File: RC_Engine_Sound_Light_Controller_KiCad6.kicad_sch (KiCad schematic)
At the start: 35 parts, among them J1 RX, J10 RGB, J11 32, J12 CH1, J13 CH2, J14 CH3, J15 ESC, J16 CH4, J2 HeadL, J3 TailL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

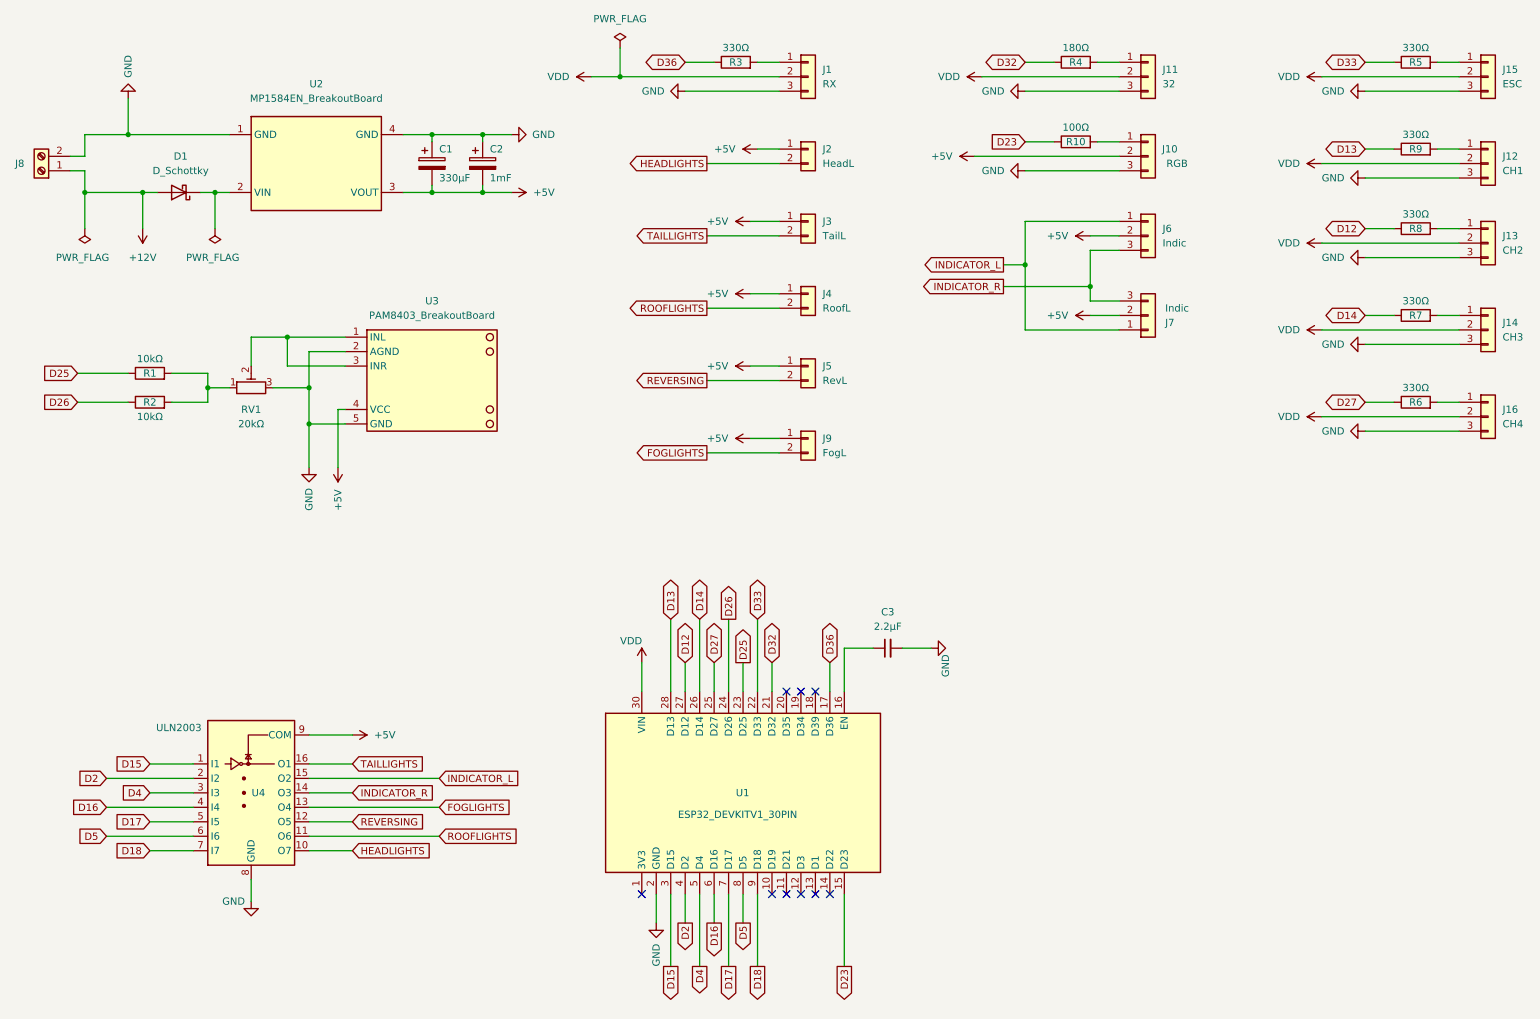
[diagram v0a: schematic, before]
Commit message: Added VDD diode.
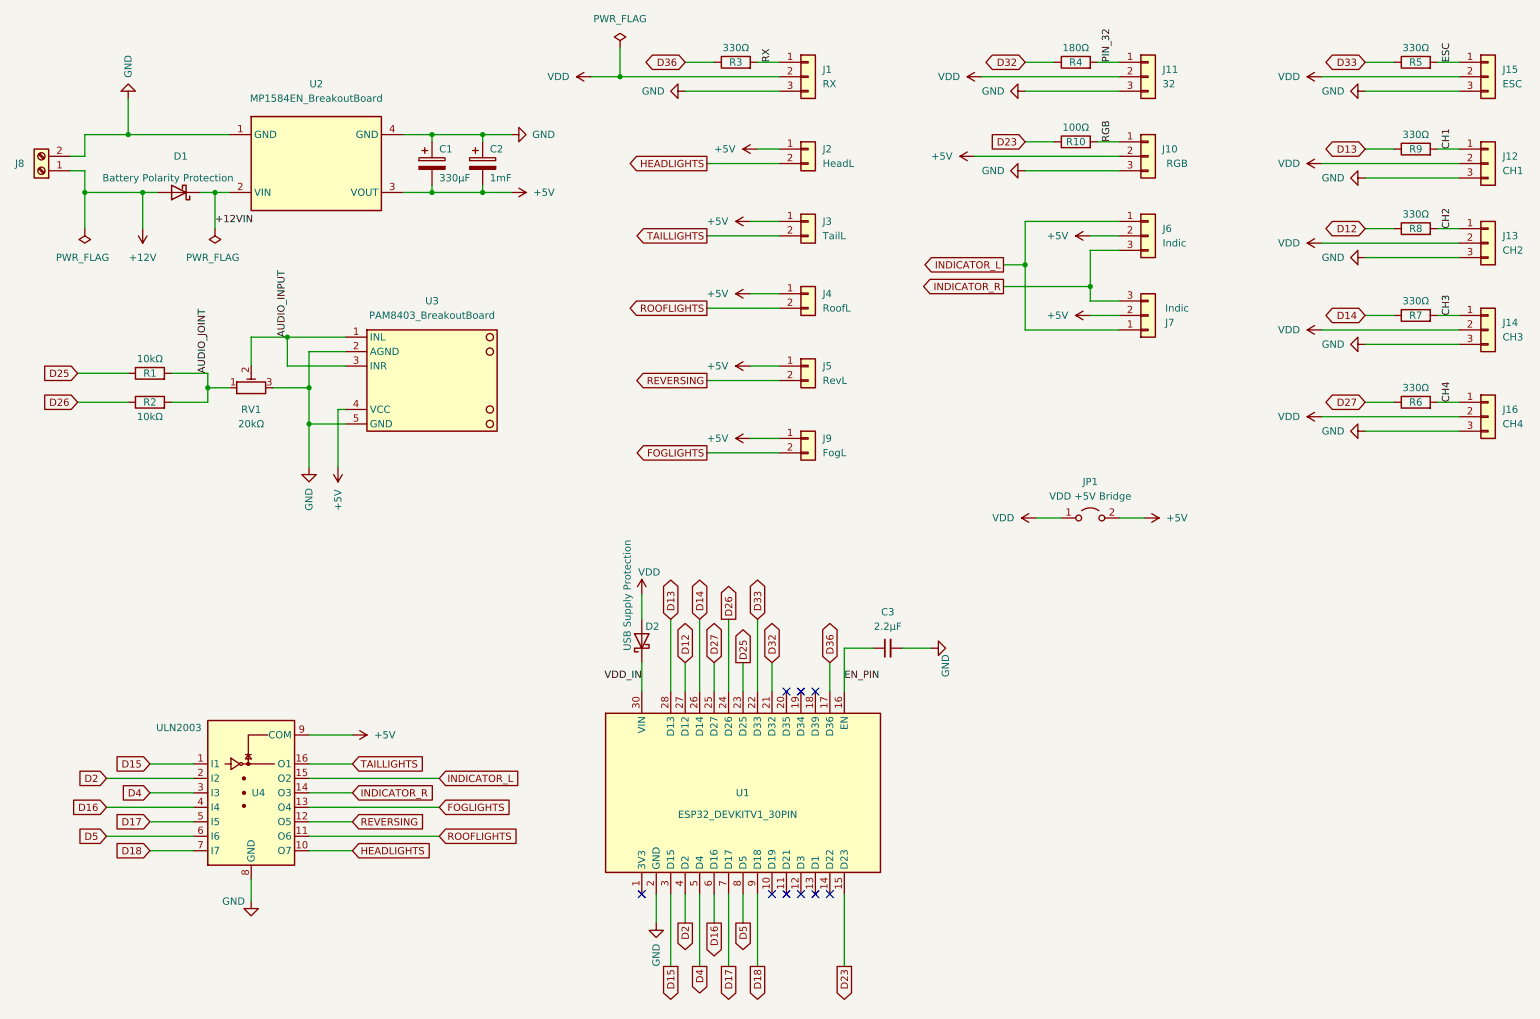
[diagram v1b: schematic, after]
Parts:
- added D2: USB Supply Protection, Diode_SMD:D_SMA, symbol Device:D_Schottky
- added JP1: VDD +5V Bridge, Connector_PinHeader_2.54mm:PinHeader_1x02_P2.54mm_Vertical, symbol Jumper:Jumper_2_Open
- D1: value D_Schottky -> Battery Polarity Protection
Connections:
- net +5V: now also JP1.2 (B)
- net VDD: now also D2.2 (A), JP1.1 (A); no longer U1.30 (VIN)
- net RX: now reaches J1.1 (Pin_1), R3.2
- net CH2: now reaches J13.1 (Pin_1), R8.2
- net AUDIO_JOINT: now reaches R1.2, R2.2, RV1.1
- net PIN_32: now reaches J11.1 (Pin_1), R4.2
- net CH1: now reaches J12.1 (Pin_1), R9.2
- net EN_PIN: now reaches C3.1, U1.16 (EN)
- net RGB: now reaches J10.1 (Pin_1), R10.2
- net +12VIN: now reaches D1.1 (K), U2.2 (VIN), U2.6 (VIN)
- net CH3: now reaches J14.1 (Pin_1), R7.2
- net ESC: now reaches J15.1 (Pin_1), R5.2
- net AUDIO_INPUT: now reaches RV1.2, U3.1 (INL), U3.3 (INR)
- net CH4: now reaches J16.1 (Pin_1), R6.2
- new net VDD_IN: D2.1 (K), U1.30 (VIN)
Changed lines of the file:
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@@
+    (stroke (width 0) (type default) (color 0 0 0 0))
+  )
+  (wire (pts (xy 124.46 116.205) (xy 124.46 120.65))
     (stroke (width 0) (type default) (color 0 0 0 0))
   )
@@
     (stroke (width 0) (type default) (color 0 0 0 0))
   )
+  (wire (pts (xy 208.28 102.87) (xy 212.725 102.87))
+    (stroke (width 0) (type default) (color 0 0 0 0))
+  )
   (wire (pts (xy 25.4 77.47) (xy 34.29 77.47))
     (stroke (width 0) (type default) (color 0 0 0 0))
@@
     (stroke (width 0) (type default) (color 0 0 0 0))
   )
+  (wire (pts (xy 193.675 102.87) (xy 198.12 102.87))
+    (stroke (width 0) (type default) (color 0 0 0 0))
+  )
   (wire (pts (xy 143.51 50.8) (xy 148.59 50.8))
     (stroke (width 0) (type default) (color 0 0 0 0))
@@
   (wire (pts (xy 157.48 128.27) (xy 157.48 133.35))
     (stroke (width 0) (type default) (color 0 0 0 0))
+  )
+  (label "VDD_IN" (at 124.46 131.445 180)
+    (effects (font (size 1.27 1.27)) (justify right bottom))
+  )
+  (label "CH3" (at 266.7 67.31 90)
+    (effects (font (size 1.27 1.27)) (justify left bottom))
+  )
+  (label "RX" (at 147.32 22.86 90)
+    (effects (font (size 1.27 1.27)) (justify left bottom))
+  )
+  (label "RGB" (at 207.01 36.83 90)
+    (effects (font (size 1.27 1.27)) (justify left bottom))
+  )
+  (label "PIN_32" (at 207.01 22.86 90)
+    (effects (font (size 1.27 1.27)) (justify left bottom))
+  )
+  (label "CH4" (at 266.7 82.55 90)
+    (effects (font (size 1.27 1.27)) (justify left bottom))
+  )
+  (label "AUDIO_INPUT" (at 62.23 71.12 90)
+    (effects (font (size 1.27 1.27)) (justify left bottom))
+  )
+  (label "CH1" (at 266.7 38.1 90)
+    (effects (font (size 1.27 1.27)) (justify left bottom))
+  )
+  (label "AUDIO_JOINT" (at 48.26 77.47 90)
+    (effects (font (size 1.27 1.27)) (justify left bottom))
+  )
+  (label "+12VIN" (at 49.53 51.435 0)
+    (effects (font (size 1.27 1.27)) (justify left bottom))
+  )
+  (label "ESC" (at 266.7 22.86 90)
+    (effects (font (size 1.27 1.27)) (justify left bottom))
+  )
+  (label "CH2" (at 266.7 52.07 90)
+    (effects (font (size 1.27 1.27)) (justify left bottom))
+  )
+  (label "EN_PIN" (at 160.02 131.445 0)
+    (effects (font (size 1.27 1.27)) (justify left bottom))
   )
   (global_label "D25" (shape input) (at 25.4 77.47 180) (fields_autoplaced)
@@
     (pin "3")
   )
+  (symbol (lib_id "Device:D_Schottky") (at 124.46 124.46 90) (unit 1)
+    (in_bom yes) (on_board yes)
+    (property "Reference" "D2" (id 0) (at 125.095 121.92 90)
+      (effects (font (size 1.27 1.27)) (justify right))
+    )
+    (property "Value" "USB Supply Protection" (id 1) (at 121.92 106.68 0)
+      (effects (font (size 1.27 1.27)) (justify right))
+    )
+    (property "Footprint" "Diode_SMD:D_SMA" (id 2) (at 124.46 124.46 0)
+      (effects (font (size 1.27 1.27)) hide)
+    )
+    (property "Datasheet" "~" (id 3) (at 124.46 124.46 0)
+      (effects (font (size 1.27 1.27)) hide)
+    )
+    (pin "1")
+    (pin "2")
+  )
   (symbol (lib_id "Connector_Generic:Conn_01x03") (at 213.36 53.34 0) (unit 1)
     (in_bom yes) (on_board yes)
@@
     (pin "2")
   )
-  (symbol (lib_id "power:VDD") (at 124.46 128.27 0) (unit 1)
-    (in_bom yes) (on_board yes)
-    (property "Reference" "#PWR0107" (id 0) (at 124.46 132.08 0)
-      (effects (font (size 1.27 1.27)) hide)
-    )
-    (property "Value" "VDD" (id 1) (at 120.65 124.46 0)
-      (effects (font (size 1.27 1.27)) (justify left))
-    )
-    (property "Footprint" "" (id 2) (at 124.46 128.27 0)
-      (effects (font (size 1.27 1.27)) hide)
-    )
-    (property "Datasheet" "" (id 3) (at 124.46 128.27 0)
+  (symbol (lib_id "power:VDD") (at 124.46 116.205 0) (unit 1)
+    (in_bom yes) (on_board yes)
+    (property "Reference" "#PWR0107" (id 0) (at 124.46 120.015 0)
+      (effects (font (size 1.27 1.27)) hide)
+    )
+    (property "Value" "VDD" (id 1) (at 123.825 112.395 0)
+      (effects (font (size 1.27 1.27)) (justify left))
+    )
+    (property "Footprint" "" (id 2) (at 124.46 116.205 0)
+      (effects (font (size 1.27 1.27)) hide)
+    )
+    (property "Datasheet" "" (id 3) (at 124.46 116.205 0)
       (effects (font (size 1.27 1.27)) hide)
     )
@@
     )
     (property "Datasheet" "" (id 3) (at 144.78 38.1 0)
+      (effects (font (size 1.27 1.27)) hide)
+    )
+    (pin "1")
+  )
+  (symbol (lib_id "power:VDD") (at 193.675 102.87 90) (unit 1)
+    (in_bom yes) (on_board yes) (fields_autoplaced)
+    (property "Reference" "#PWR0114" (id 0) (at 197.485 102.87 0)
+      (effects (font (size 1.27 1.27)) hide)
+    )
+    (property "Value" "VDD" (id 1) (at 189.865 102.8699 90)
+      (effects (font (size 1.27 1.27)) (justify left))
+    )
+    (property "Footprint" "" (id 2) (at 193.675 102.87 0)
+      (effects (font (size 1.27 1.27)) hide)
+    )
+    (property "Datasheet" "" (id 3) (at 193.675 102.87 0)
       (effects (font (size 1.27 1.27)) hide)
     )
@@
     (pin "2")
   )
+  (symbol (lib_id "power:+5V") (at 212.725 102.87 270) (unit 1)
+    (in_bom yes) (on_board yes) (fields_autoplaced)
+    (property "Reference" "#PWR0136" (id 0) (at 208.915 102.87 0)
+      (effects (font (size 1.27 1.27)) hide)
+    )
+    (property "Value" "+5V" (id 1) (at 216.535 102.8699 90)
+      (effects (font (size 1.27 1.27)) (justify left))
+    )
+    (property "Footprint" "" (id 2) (at 212.725 102.87 0)
+      (effects (font (size 1.27 1.27)) hide)
+    )
+    (property "Datasheet" "" (id 3) (at 212.725 102.87 0)
+      (effects (font (size 1.27 1.27)) hide)
+    )
+    (pin "1")
+  )
   (symbol (lib_id "power:PWR_FLAG") (at 26.67 52.07 180) (unit 1)
     (in_bom yes) (on_board yes)
@@
     )
     (pin "1")
+  )
+  (symbol (lib_id "Jumper:Jumper_2_Open") (at 203.2 102.87 0) (unit 1)
+    (in_bom yes) (on_board yes) (fields_autoplaced)
+    (property "Reference" "JP1" (id 0) (at 203.2 96.52 0))
+    (property "Value" "VDD +5V Bridge" (id 1) (at 203.2 99.06 0))
+    (property "Footprint" "Connector_PinHeader_2.54mm:PinHeader_1x02_P2.54mm_Vertical" (id 2) (at 203.2 102.87 0)
+      (effects (font (size 1.27 1.27)) hide)
+    )
+    (property "Datasheet" "~" (id 3) (at 203.2 102.87 0)
+      (effects (font (size 1.27 1.27)) hide)
+    )
+    (pin "1")
+    (pin "2")
   )
   (symbol (lib_id "power:+5V") (at 71.12 93.98 180) (unit 1)
@@
   )
   (symbol (lib_id "Device:D_Schottky") (at 43.18 45.72 180) (unit 1)
-    (in_bom yes) (on_board yes) (fields_autoplaced)
+    (in_bom yes) (on_board yes)
     (property "Reference" "D1" (id 0) (at 43.4975 39.37 0))
-    (property "Value" "D_Schottky" (id 1) (at 43.4975 41.91 0))
+    (property "Value" "Battery Polarity Protection" (id 1) (at 41.275 43.18 0))
     (property "Footprint" "Diode_SMD:D_SMA-SMB_Universal_Handsoldering" (id 2) (at 43.18 45.72 0)
       (effects (font (size 1.27 1.27)) hide)
@@
       (reference "#PWR0113") (unit 1) (value "GND") (footprint "")
     )
+    (path "/2c0a5d94-853e-4fc7-89e4-5e30e747050f"
+      (reference "#PWR0114") (unit 1) (value "VDD") (footprint "")
+    )
     (path "/c3e6ee58-5986-4571-bfc1-b1e317eeebeb"
       (reference "#PWR0115") (unit 1) (value "GND") (footprint "")
@@
       (reference "#PWR0135") (unit 1) (value "GND") (footprint "")
     )
+    (path "/2fe8b2a2-3f98-440d-af7a-40fe3be4e184"
+      (reference "#PWR0136") (unit 1) (value "+5V") (footprint "")
+    )
     (path "/3c5fb390-8090-4852-843b-532aeb1c18b0"
       (reference "C1") (unit 1) (value "330µF") (footprint "Capacitor_Tantalum_SMD:CP_EIA-7343-30_AVX-N_Pad2.25x2.55mm_HandSolder")
@@
     )
     (path "/eca3bb7b-a37d-4395-81c5-81f63a2b25c0"
-      (reference "D1") (unit 1) (value "D_Schottky") (footprint "Diode_SMD:D_SMA-SMB_Universal_Handsoldering")
+      (reference "D1") (unit 1) (value "Battery Polarity Protection") (footprint "Diode_SMD:D_SMA-SMB_Universal_Handsoldering")
+    )
+    (path "/06c0930c-a18e-4fca-b8a3-f528b2e22414"
+      (reference "D2") (unit 1) (value "USB Supply Protection") (footprint "Diode_SMD:D_SMA")
     )
     (path "/03b5281b-f2b9-42ca-84a7-e7f14e3aaaa5"
@@
       (reference "J16") (unit 1) (value "CH4") (footprint "Connector_PinHeader_2.54mm:PinHeader_1x03_P2.54mm_Vertical")
     )
+    (path "/47cd2bdc-a2cb-4914-b692-4cd168710091"
+      (reference "JP1") (unit 1) (value "VDD +5V Bridge") (footprint "Connector_PinHeader_2.54mm:PinHeader_1x02_P2.54mm_Vertical")
+    )
     (path "/b13367e3-bbbc-4c81-beb3-d8762f1fd4c0"

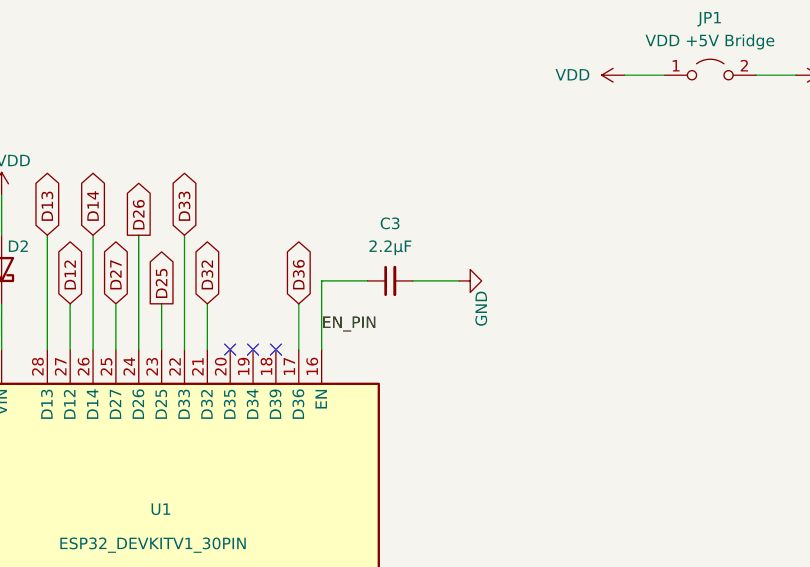
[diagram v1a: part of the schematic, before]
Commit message: Removed EN cap, added USB diode.
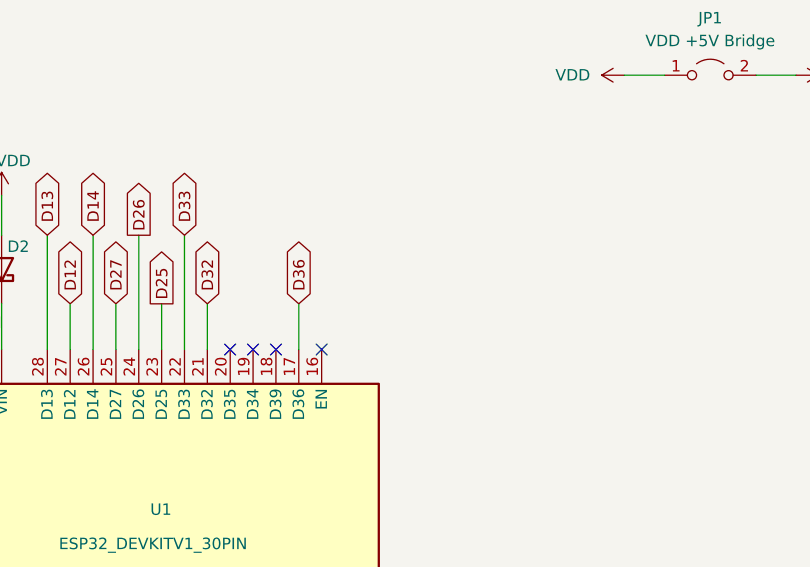
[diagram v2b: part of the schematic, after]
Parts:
- removed C3: 2.2µF, Capacitor_SMD:C_1206_3216Metric_Pad1.33x1.80mm_HandSolder, symbol Device:C_Small
- D1: footprint Diode_SMD:D_SMA-SMB_Universal_Handsoldering -> Diode_SMD:D_SMA_Handsoldering
- D2: footprint Diode_SMD:D_SMA -> Diode_SMD:D_SMA_Handsoldering
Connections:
- net EN_PIN: no longer names the net of U1.16 (EN)
- no-connect marks 9 -> 10
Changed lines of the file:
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@@
   (junction (at 120.65 25.4) (diameter 0) (color 0 0 0 0)
   )
+  (no_connect (at 160.02 133.35))
   (no_connect (at 154.94 133.35))
   (no_connect (at 149.86 133.35))
@@
     (stroke (width 0) (type default) (color 0 0 0 0))
   )
-  (wire (pts (xy 160.02 133.35) (xy 160.02 125.73))
-    (stroke (width 0) (type default) (color 0 0 0 0))
-  )
   (wire (pts (xy 24.13 39.37) (xy 26.67 39.37))
     (stroke (width 0) (type default) (color 0 0 0 0))
@@
     (stroke (width 0) (type default) (color 0 0 0 0))
   )
-  (wire (pts (xy 170.18 125.73) (xy 175.26 125.73))
-    (stroke (width 0) (type default) (color 0 0 0 0))
-  )
   (wire (pts (xy 66.04 156.21) (xy 73.66 156.21))
     (stroke (width 0) (type default) (color 0 0 0 0))
@@
   )
   (wire (pts (xy 182.88 39.37) (xy 208.28 39.37))
-    (stroke (width 0) (type default) (color 0 0 0 0))
-  )
-  (wire (pts (xy 160.02 125.73) (xy 165.1 125.73))
     (stroke (width 0) (type default) (color 0 0 0 0))
   )
@@
   )
   (label "CH2" (at 266.7 52.07 90)
-    (effects (font (size 1.27 1.27)) (justify left bottom))
-  )
-  (label "EN_PIN" (at 160.02 131.445 0)
     (effects (font (size 1.27 1.27)) (justify left bottom))
   )
@@
       (effects (font (size 1.27 1.27)) (justify right))
     )
-    (property "Footprint" "Diode_SMD:D_SMA" (id 2) (at 124.46 124.46 0)
+    (property "Footprint" "Diode_SMD:D_SMA_Handsoldering" (id 2) (at 124.46 124.46 0)
       (effects (font (size 1.27 1.27)) hide)
     )
@@
     )
     (pin "1")
-  )
-  (symbol (lib_id "Device:C_Small") (at 167.64 125.73 90) (unit 1)
-    (in_bom yes) (on_board yes) (fields_autoplaced)
-    (property "Reference" "C3" (id 0) (at 167.6463 119.38 90))
-    (property "Value" "2.2µF" (id 1) (at 167.6463 121.92 90))
-    (property "Footprint" "Capacitor_SMD:C_1206_3216Metric_Pad1.33x1.80mm_HandSolder" (id 2) (at 167.64 125.73 0)
-      (effects (font (size 1.27 1.27)) hide)
-    )
-    (property "Datasheet" "~" (id 3) (at 167.64 125.73 0)
-      (effects (font (size 1.27 1.27)) hide)
-    )
-    (pin "1")
-    (pin "2")
   )
   (symbol (lib_id "power:VDD") (at 243.84 85.09 90) (unit 1)
@@
     )
     (property "Datasheet" "" (id 3) (at 243.84 54.61 0)
-      (effects (font (size 1.27 1.27)) hide)
-    )
-    (pin "1")
-  )
-  (symbol (lib_id "power:GND") (at 175.26 125.73 90) (unit 1)
-    (in_bom yes) (on_board yes)
-    (property "Reference" "#PWR0113" (id 0) (at 181.61 125.73 0)
-      (effects (font (size 1.27 1.27)) hide)
-    )
-    (property "Value" "GND" (id 1) (at 177.8 130.81 0)
-      (effects (font (size 1.27 1.27)) (justify left))
-    )
-    (property "Footprint" "" (id 2) (at 175.26 125.73 0)
-      (effects (font (size 1.27 1.27)) hide)
-    )
-    (property "Datasheet" "" (id 3) (at 175.26 125.73 0)
       (effects (font (size 1.27 1.27)) hide)
     )
@@
     (property "Reference" "D1" (id 0) (at 43.4975 39.37 0))
     (property "Value" "Battery Polarity Protection" (id 1) (at 41.275 43.18 0))
-    (property "Footprint" "Diode_SMD:D_SMA-SMB_Universal_Handsoldering" (id 2) (at 43.18 45.72 0)
+    (property "Footprint" "Diode_SMD:D_SMA_Handsoldering" (id 2) (at 43.18 45.72 0)
       (effects (font (size 1.27 1.27)) hide)
     )
@@
       (reference "#PWR0112") (unit 1) (value "GND") (footprint "")
     )
-    (path "/8954f574-61fe-4e29-8bfc-13436fd54371"
-      (reference "#PWR0113") (unit 1) (value "GND") (footprint "")
-    )
     (path "/2c0a5d94-853e-4fc7-89e4-5e30e747050f"
       (reference "#PWR0114") (unit 1) (value "VDD") (footprint "")
@@
       (reference "C2") (unit 1) (value "1mF") (footprint "Capacitor_THT:CP_Radial_D10.0mm_P2.50mm_P5.00mm")
     )
-    (path "/5c3e35df-d9b1-4b11-95d1-3f2d221feff7"
-      (reference "C3") (unit 1) (value "2.2µF") (footprint "Capacitor_SMD:C_1206_3216Metric_Pad1.33x1.80mm_HandSolder")
-    )
     (path "/eca3bb7b-a37d-4395-81c5-81f63a2b25c0"
-      (reference "D1") (unit 1) (value "Battery Polarity Protection") (footprint "Diode_SMD:D_SMA-SMB_Universal_Handsoldering")
+      (reference "D1") (unit 1) (value "Battery Polarity Protection") (footprint "Diode_SMD:D_SMA_Handsoldering")
     )
     (path "/06c0930c-a18e-4fca-b8a3-f528b2e22414"
-      (reference "D2") (unit 1) (value "USB Supply Protection") (footprint "Diode_SMD:D_SMA")
+      (reference "D2") (unit 1) (value "USB Supply Protection") (footprint "Diode_SMD:D_SMA_Handsoldering")
     )
     (path "/03b5281b-f2b9-42ca-84a7-e7f14e3aaaa5"
